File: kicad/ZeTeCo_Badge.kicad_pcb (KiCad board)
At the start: 2 copper layers, 75 x 75 mm, 118 parts, among them J1 GPIO, J12 Bat. (+), J13 Bat. (-), J15 USB_A, J2 3V, Q1 2N7002, Q2 2N7002, Q3 2N7002, Q4 2N7002, U1 ATTINY85-20S

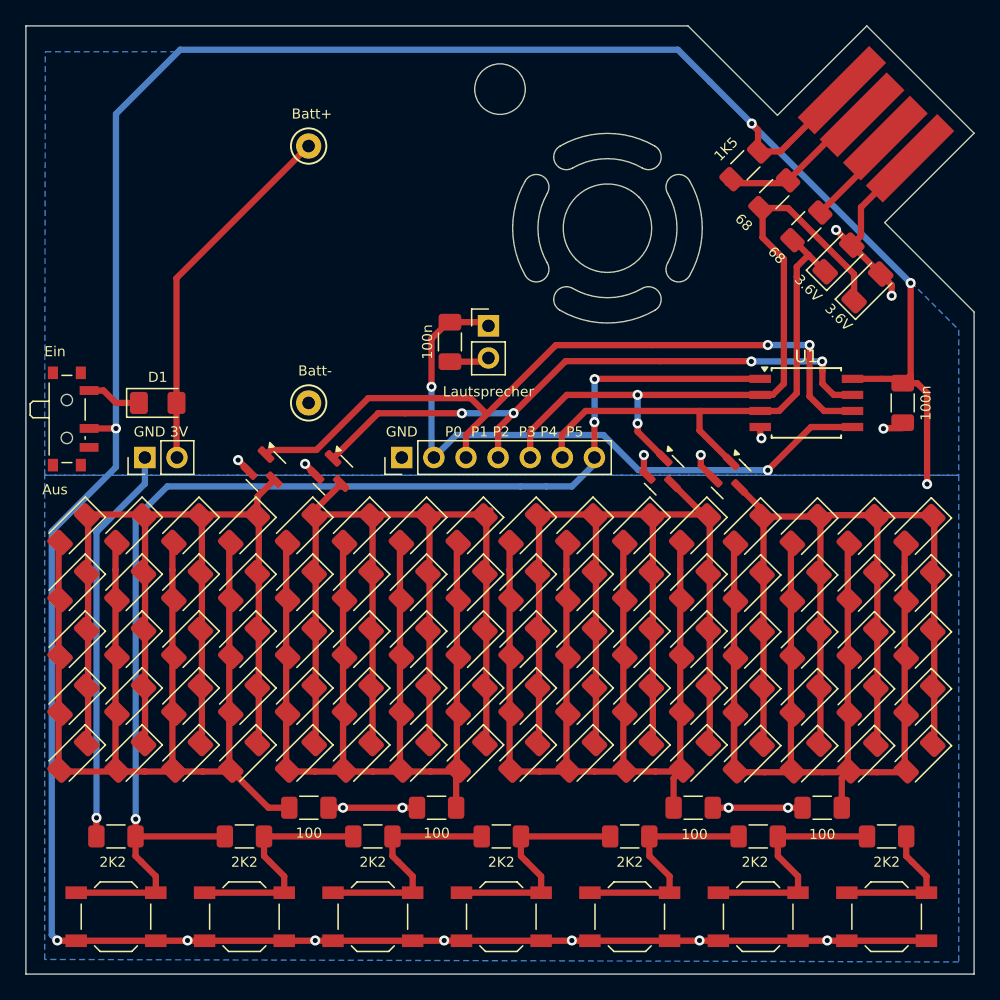
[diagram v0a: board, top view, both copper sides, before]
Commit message: Replace PCB text with component values on silkscreen
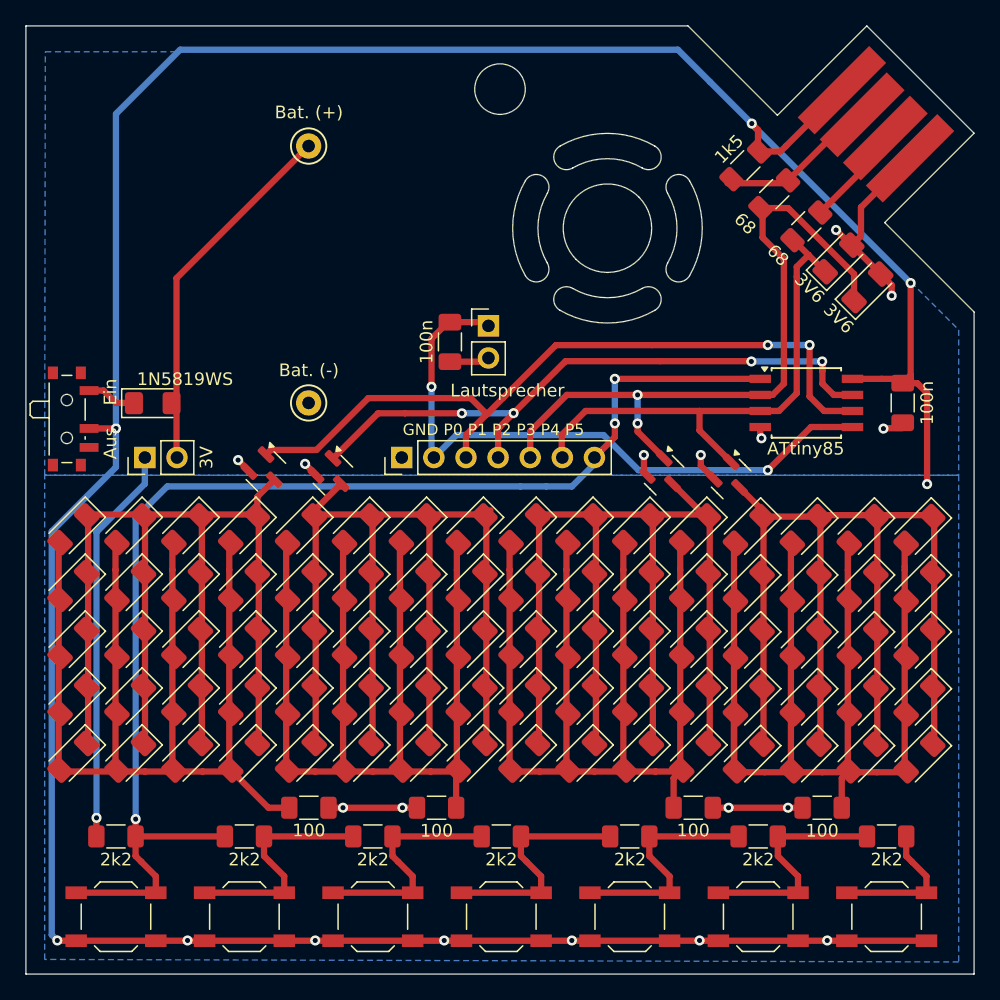
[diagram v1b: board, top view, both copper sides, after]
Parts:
- D1: value D -> 1N5819WS
- J1: value GPIO -> GND P0 P1 P2 P3 P4 P5
- JP9: value Aus/Ein -> Aus Ein
- LS1: value Speaker -> Lautsprecher
- U1: value ATTINY85-20S -> ATtiny85
- moved D1 0.39 mm to (183.2, 81.3)
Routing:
- net Net-(J1-Pin_7): track 101.5 -> 100.6 mm
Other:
- board text removed: "100"
- board text removed: "100n"
- board text removed: "1K5"
- board text removed: "2K2"
- board text removed: "3.6V"
- board text removed: "68"
- board text removed: "Aus"
- board text removed: "Batt+"
- board text removed: "Batt-"
- board text removed: "D1"
- board text removed: "Ein"
- board text removed: "GND"
- board text removed: "GND 3V"
- board text removed: "Lautsprecher"
- board text removed: "P0 P1 P2 P3 P4 P5"
